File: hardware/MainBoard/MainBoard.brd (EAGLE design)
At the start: 90 x 56 mm, 220 parts, among them J1 CON-71741-2184-BOT, J2 CON-71741-2184-TOP, J3 CON-FTSH-105-01-L-DV-K, J4 CON-ZX62R-B-5P, J5 CON-SMA, J6 CON-SMA, J7 CON-RJ45-J0G-0007NL, J8 SWITCH-CJS-1200-1200, M1 MOUNT-HOLE3.3, M2 MOUNT-HOLE3.3, M3 MOUNT-HOLE3.3, M4 MOUNT-HOLE3.3, M5 FIDUCIAL1X2, M6 FIDUCIAL1X2, M7 FIDUCIAL1X2, M8 FIDUCIAL1X2, Q1 MMBT3904, SW1 SWITCH-KSC-201J, SW2 SWITCH-KSC-201J, U1 A2F500M3G-FG256, U2 MAX19706-T4877-4, U3 MAX19706-T4877-4, U4 USBLC6-2SC6, U5 FT232HL, U6 DP83848C-VBH48A, U7 93LC56BT-OT, U8 DS1818-10-SOT-23, U9 LMV112, X1 FOX924B, X2 ECX-31B, X3 ASEM1-C, X5 ECX-42-120

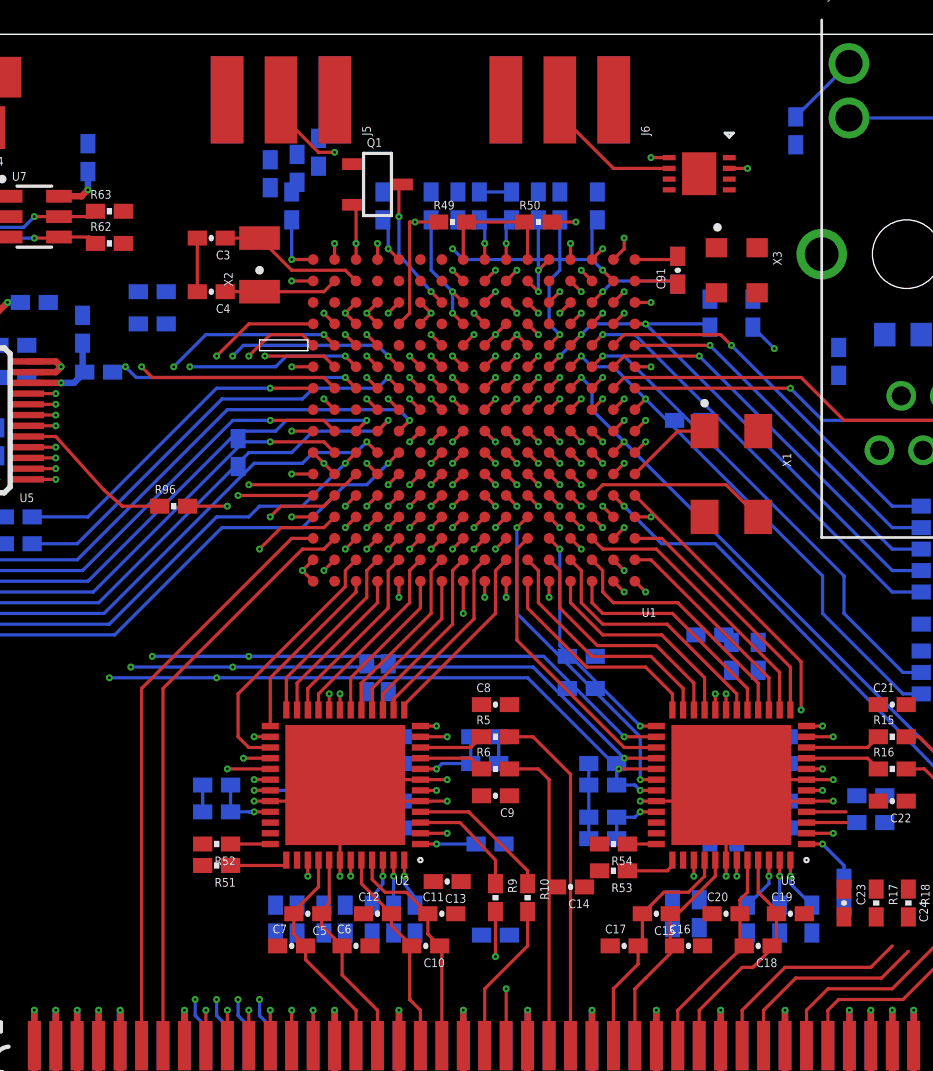
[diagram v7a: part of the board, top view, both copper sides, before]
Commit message: Starting add FPGA supply decoupling capacitors.
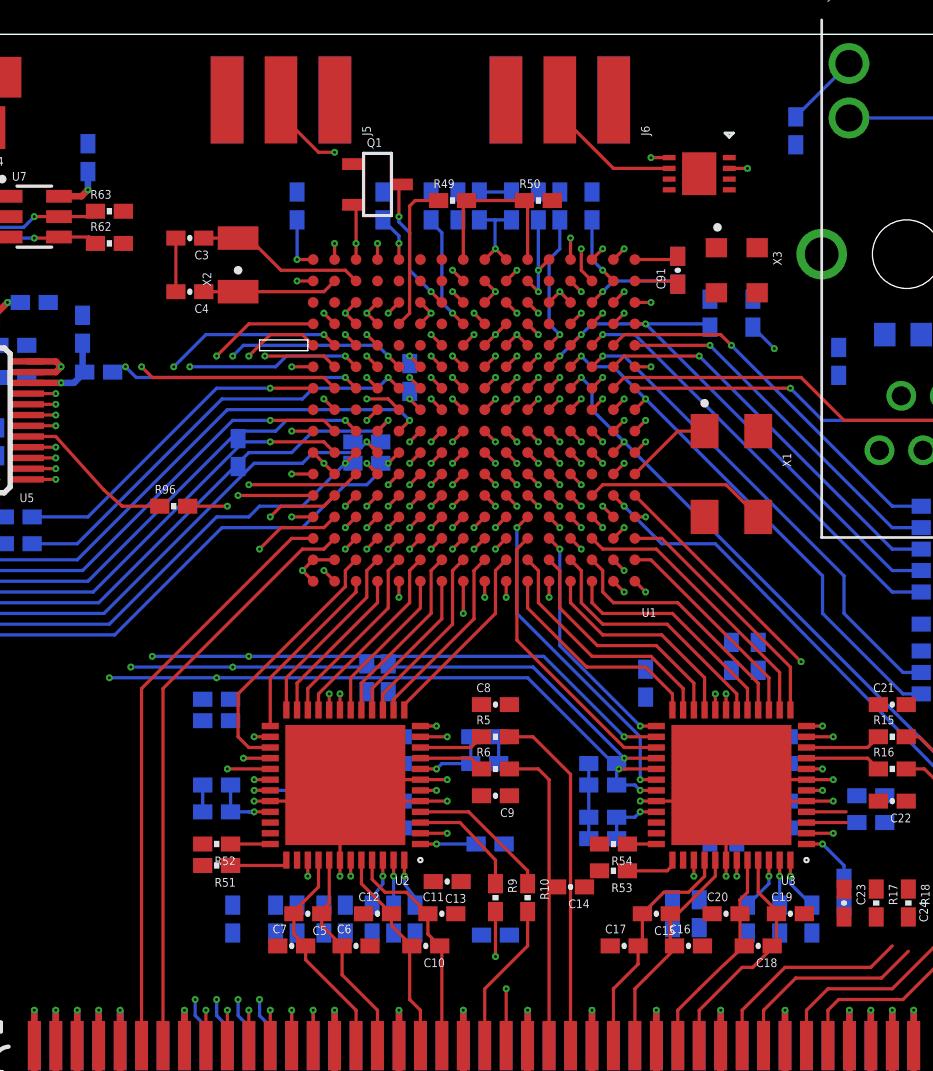
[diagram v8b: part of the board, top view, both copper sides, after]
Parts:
- moved R21 31.5 mm to (33.8, 14.8), turned to 90 degrees
- moved R19 19.2 mm to (33.0, 25.0), turned to 180 degrees
- moved R20 18.7 mm to (33.0, 24.0), turned to 180 degrees
- moved C76 14.1 mm to (40.0, 36.0), turned to 0 degrees
- moved C75 13.7 mm to (40.0, 37.0), turned to 0 degrees
- moved C74 11.5 mm to (42.0, 40.0), turned to 90 degrees
- moved R25 6.75 mm to (56.0, 21.2), turned to 180 degrees
- moved R24 6.60 mm to (56.0, 22.8)
- moved R23 3.25 mm to (53.0, 25.8), turned to 270 degrees
- moved C3 1.00 mm to (31.8, 46.5)
- moved C4 1.00 mm to (31.8, 44.0)
- moved R49 1.00 mm to (44.0, 48.2)
- moved R50 1.00 mm to (48.0, 48.2)
- moved X2 1.00 mm to (34.0, 45.2)
- moved C66 0.25 mm to (50.5, 48.0)
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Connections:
- net NGPIO0: now also U1.G2; no longer U1.G3
- net SGPIO0: now also U1.J3; no longer U1.H2
- net SGPIO1: now also U1.H2; no longer U1.G1
- net SGPIO2: now also U1.G1; no longer U1.J3
- net SGPIO3: now also U1.G3; no longer U1.G2
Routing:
- net SGPIO0: track 41.0 -> 48.9 mm
- net SGPIO1: track 39.8 -> 46.9 mm
- net SGPIO2: track 49.0 -> 45.8 mm
- net VAREFIN: track 7.76 -> 9.76 mm
- net NGPIO0: track 42.6 -> 44.5 mm
- net SF_TM0: track 50.1 -> 48.7 mm
- net A3V3: track 53.2 -> 51.9 mm, vias 28 -> 27
- net SF_ABPS1: track 51.4 -> 50.1 mm
- net SF_ABPS0: track 55.8 -> 54.5 mm
- net D3V3: track 38.8 -> 39.9 mm, vias 27 -> 29
- net LPXIN: track 6.93 -> 7.93 mm
- net TDI: track 36.5 -> 35.5 mm
- net LPXOUT: track 5.31 -> 6.31 mm
- net AGND: track 258.2 -> 257.3 mm, vias 45 -> 43
- net EXT_CLK_IN: track 29.0 -> 28.1 mm
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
